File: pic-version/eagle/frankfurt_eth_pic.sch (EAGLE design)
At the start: 60 parts, among them IC1 PIC18F26K80, IC2 ENC28J60-SO, IC3 SN65HVD232, IC4 LM2575S, IC5 11AA02E48, IC6 MCP23A256, IC7 AT45DB041D, J2 A00-108-220-450, Q1 10 MHz, Q2 25 MHz

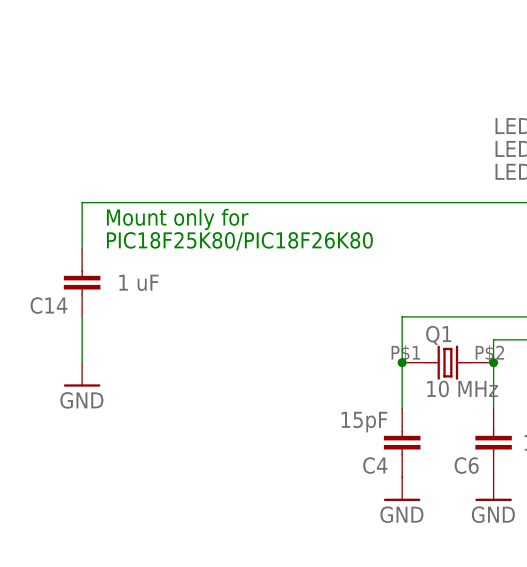
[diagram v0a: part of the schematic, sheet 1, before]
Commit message: Changed value of C14 to 10uF
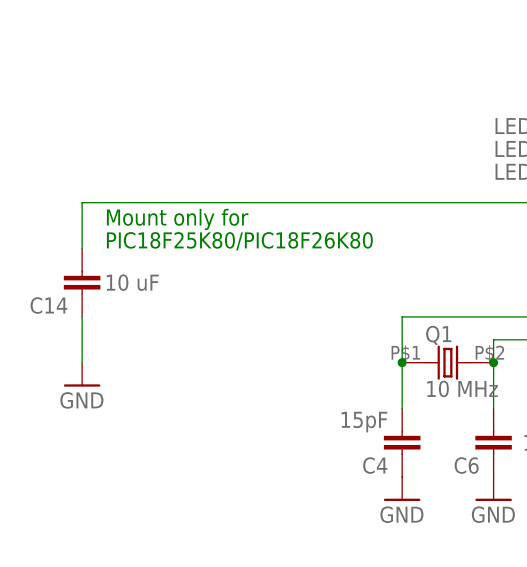
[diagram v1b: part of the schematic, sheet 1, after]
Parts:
- C14: value 1 uF -> 10 uF
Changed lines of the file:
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@@
 <part name="LED2" library="led" deviceset="LED" device="CHIP-LED0805" value="Red LED"/>
 <part name="P+9" library="SUPPLY1" deviceset="VCC" device=""/>
-<part name="C14" library="rcl" deviceset="C-EU" device="C0805" value="1 uF"/>
+<part name="C14" library="rcl" deviceset="C-EU" device="C0805" value="10 uF"/>
 <part name="GND32" library="SUPPLY1" deviceset="GND" device=""/>
 <part name="R17" library="rcl" deviceset="R-EU_" device="R0805" value="120"/>
